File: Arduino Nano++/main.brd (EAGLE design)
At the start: 83.2 x 53.3 mm, 64 parts, among them IC1 LM358N, Q1 IRF9530, Q2 IRF9530

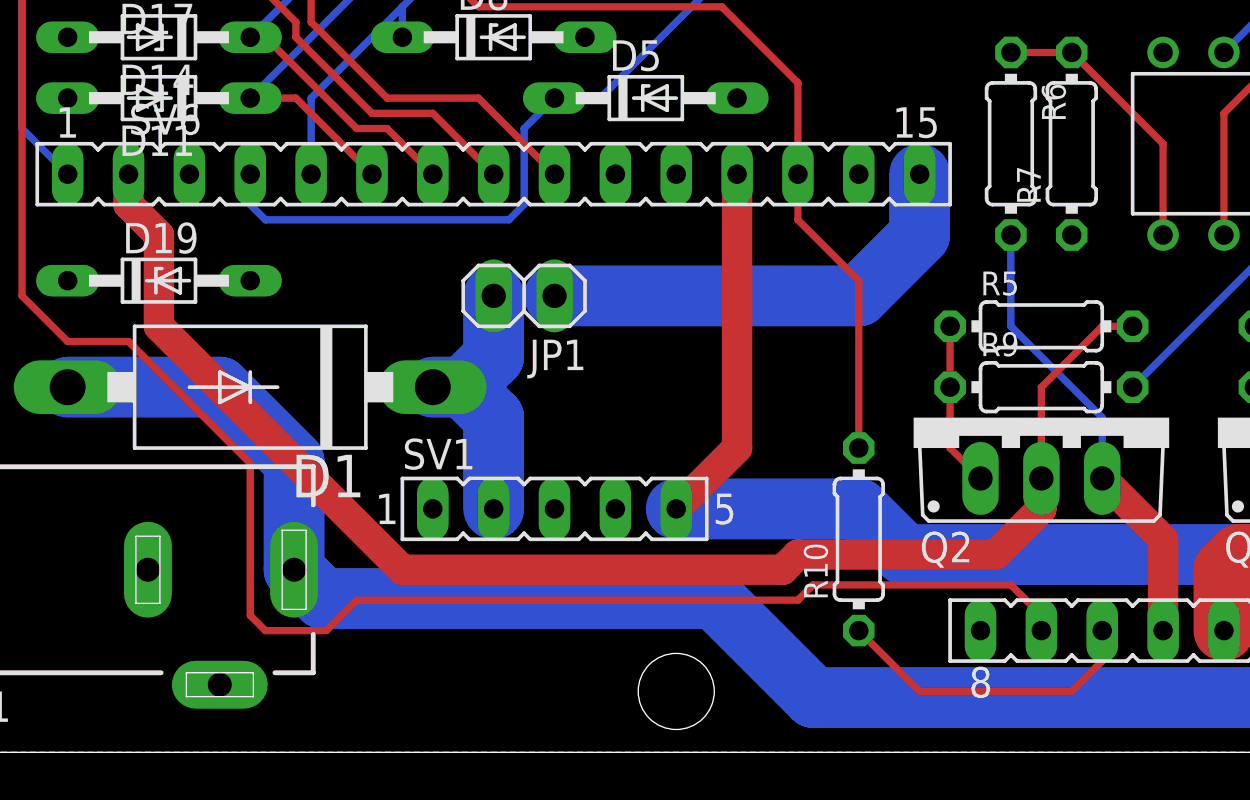
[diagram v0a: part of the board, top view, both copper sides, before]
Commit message: Increased vreg clearance
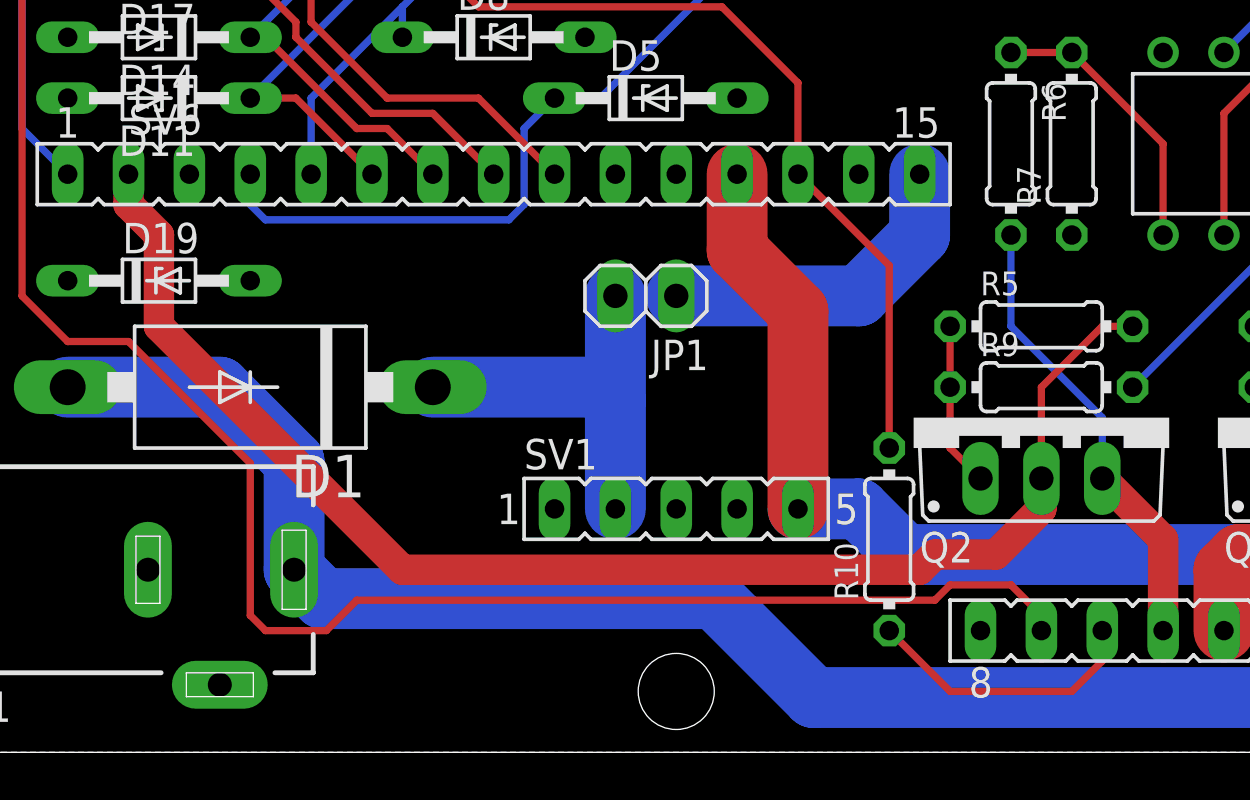
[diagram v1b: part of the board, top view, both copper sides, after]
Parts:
- moved JP1 5.08 mm to (27.9, 39.4)
- moved SV1 5.08 mm to (29.2, 30.5)
- moved R10 1.27 mm to (38.1, 29.2)
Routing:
- net N$2: track 11.2 -> 16.7 mm
- net VIN: track 18.8 -> 13.8 mm
- net 5V: track 69.8 -> 64.7 mm
- net RST': track 13.0 -> 11.7 mm
- net RST: track 46.8 -> 47.3 mm
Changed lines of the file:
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@@
 </element>
 <element name="IC1" library="linear" library_urn="urn:adsk.eagle:library:262" package="DIL08" package3d_urn="urn:adsk.eagle:package:16409/1" value="LM358N" x="53.34" y="45.72" rot="R180"/>
-<element name="JP1" library="pinhead" library_urn="urn:adsk.eagle:library:325" package="1X02" package3d_urn="urn:adsk.eagle:package:22435/2" value="" x="22.86" y="39.37" rot="R180"/>
+<element name="JP1" library="pinhead" library_urn="urn:adsk.eagle:library:325" package="1X02" package3d_urn="urn:adsk.eagle:package:22435/2" value="" x="27.94" y="39.37" rot="R180"/>
 <element name="SV6" library="con-lsta" library_urn="urn:adsk.eagle:library:161" package="FE15" package3d_urn="urn:adsk.eagle:package:8206/1" value="" x="21.59" y="44.45">
 <attribute name="MF" value="" x="21.59" y="44.45" size="1.778" layer="27" display="off"/>
@@
 <element name="R5" library="rcl" library_urn="urn:adsk.eagle:library:334" package="0204/7" package3d_urn="urn:adsk.eagle:package:23498/1" value="10k" x="44.45" y="38.1"/>
 <element name="R9" library="rcl" library_urn="urn:adsk.eagle:library:334" package="0204/7" package3d_urn="urn:adsk.eagle:package:23498/1" value="300" x="44.45" y="35.56"/>
-<element name="R10" library="rcl" library_urn="urn:adsk.eagle:library:334" package="0204/7" package3d_urn="urn:adsk.eagle:package:23498/1" value="1k" x="36.83" y="29.21" rot="R90"/>
-<element name="SV1" library="con-lsta" library_urn="urn:adsk.eagle:library:161" package="FE05-1" package3d_urn="urn:adsk.eagle:package:8190/1" value="" x="24.13" y="30.48">
-<attribute name="MF" value="" x="24.13" y="30.48" size="1.778" layer="27" display="off"/>
-<attribute name="MPN" value="" x="24.13" y="30.48" size="1.778" layer="27" display="off"/>
-<attribute name="OC_FARNELL" value="unknown" x="24.13" y="30.48" size="1.778" layer="27" display="off"/>
-<attribute name="OC_NEWARK" value="unknown" x="24.13" y="30.48" size="1.778" layer="27" display="off"/>
+<element name="R10" library="rcl" library_urn="urn:adsk.eagle:library:334" package="0204/7" package3d_urn="urn:adsk.eagle:package:23498/1" value="1k" x="38.1" y="29.21" rot="R90"/>
+<element name="SV1" library="con-lsta" library_urn="urn:adsk.eagle:library:161" package="FE05-1" package3d_urn="urn:adsk.eagle:package:8190/1" value="" x="29.21" y="30.48">
+<attribute name="MF" value="" x="29.21" y="30.48" size="1.778" layer="27" display="off"/>
+<attribute name="MPN" value="" x="29.21" y="30.48" size="1.778" layer="27" display="off"/>
+<attribute name="OC_FARNELL" value="unknown" x="29.21" y="30.48" size="1.778" layer="27" display="off"/>
+<attribute name="OC_NEWARK" value="unknown" x="29.21" y="30.48" size="1.778" layer="27" display="off"/>
 </element>
 <element name="SV3" library="con-lsta" library_urn="urn:adsk.eagle:library:161" package="FE06" package3d_urn="urn:adsk.eagle:package:8191/1" value="" x="71.12" y="25.4" rot="R180">
@@
 <wire x1="6.35" y1="43.18" x2="7.62" y2="41.91" width="1.27" layer="1"/>
 <wire x1="7.62" y1="38.1" x2="7.62" y2="41.91" width="1.27" layer="1"/>
-<wire x1="42.545" y1="28.575" x2="34.29" y2="28.575" width="1.27" layer="1"/>
 <wire x1="42.545" y1="28.575" x2="44.45" y2="30.48" width="1.27" layer="1"/>
 <wire x1="44.45" y1="31.75" x2="44.45" y2="30.48" width="1.27" layer="1"/>
-<wire x1="34.29" y1="28.575" x2="33.655" y2="27.94" width="1.27" layer="1"/>
-<wire x1="33.655" y1="27.94" x2="17.78" y2="27.94" width="1.27" layer="1"/>
-<wire x1="17.78" y1="27.94" x2="7.62" y2="38.1" width="1.27" layer="1"/>
+<wire x1="7.62" y1="38.1" x2="17.78" y2="27.94" width="1.27" layer="1"/>
 <wire x1="48.26" y1="38.1" x2="46.99" y2="38.1" width="0.3048" layer="1"/>
 <wire x1="46.99" y1="38.1" x2="44.45" y2="35.56" width="0.3048" layer="1"/>
 <wire x1="44.45" y1="35.56" x2="44.45" y2="31.75" width="0.3048" layer="1"/>
+<wire x1="39.37" y1="27.94" x2="40.005" y2="28.575" width="1.27" layer="1"/>
+<wire x1="40.005" y1="28.575" x2="42.545" y2="28.575" width="1.27" layer="1"/>
+<wire x1="17.78" y1="27.94" x2="39.37" y2="27.94" width="1.27" layer="1"/>
 </signal>
 <signal name="5V">
@@
 <contactref element="SV1" pad="5"/>
 <contactref element="IC1" pad="8"/>
-<wire x1="29.21" y1="30.48" x2="36.83" y2="30.48" width="2.54" layer="16"/>
+<wire x1="34.29" y1="30.48" x2="36.83" y2="30.48" width="2.54" layer="16"/>
 <wire x1="36.83" y1="30.48" x2="38.735" y2="28.575" width="2.54" layer="16"/>
 <wire x1="38.735" y1="28.575" x2="56.515" y2="28.575" width="2.54" layer="16"/>
 <wire x1="56.515" y1="28.575" x2="57.15" y2="29.21" width="2.54" layer="16"/>
 <wire x1="57.15" y1="29.21" x2="57.15" y2="31.75" width="2.54" layer="16"/>
-<wire x1="29.21" y1="30.48" x2="31.75" y2="33.02" width="1.27" layer="1"/>
-<wire x1="31.75" y1="33.02" x2="31.75" y2="44.45" width="1.27" layer="1"/>
 <wire x1="59.69" y1="38.1" x2="60.96" y2="38.1" width="0.3048" layer="1"/>
 <wire x1="59.69" y1="38.1" x2="57.15" y2="35.56" width="0.3048" layer="1"/>
@@
 <wire x1="60.96" y1="38.1" x2="63.5" y2="38.1" width="0.3048" layer="1"/>
 <wire x1="63.5" y1="38.1" x2="68.58" y2="43.18" width="0.3048" layer="1"/>
+<wire x1="34.29" y1="30.48" x2="34.29" y2="38.735" width="2.54" layer="1"/>
+<wire x1="34.29" y1="38.735" x2="31.75" y2="41.275" width="2.54" layer="1"/>
+<wire x1="31.75" y1="41.275" x2="31.75" y2="44.45" width="2.54" layer="1"/>
 </signal>
 <signal name="GND">
@@
 <contactref element="SV4" pad="1"/>
 <wire x1="44.45" y1="25.4" x2="44.45" y2="26.035" width="0.3048" layer="1"/>
-<wire x1="44.45" y1="26.035" x2="43.18" y2="27.305" width="0.3048" layer="1"/>
-<wire x1="43.18" y1="27.305" x2="34.925" y2="27.305" width="0.3048" layer="1"/>
-<wire x1="34.925" y1="27.305" x2="34.29" y2="26.67" width="0.3048" layer="1"/>
-<wire x1="34.29" y1="26.67" x2="15.875" y2="26.67" width="0.3048" layer="1"/>
-<wire x1="15.875" y1="26.67" x2="14.605" y2="25.4" width="0.3048" layer="1"/>
+<wire x1="43.186896875" y1="27.298103125" x2="44.45" y2="26.035" width="0.3048" layer="1"/>
+<wire x1="43.186896875" y1="27.298103125" x2="43.18" y2="27.305" width="0.3048" layer="1"/>
+<wire x1="14.605" y1="25.4" x2="15.875" y2="26.67" width="0.3048" layer="1"/>
 <wire x1="14.605" y1="25.4" x2="12.065" y2="25.4" width="0.3048" layer="1"/>
 <wire x1="12.065" y1="25.4" x2="11.43" y2="26.035" width="0.3048" layer="1"/>
@@
 <wire x1="33.655" y1="66.675" x2="38.1" y2="71.12" width="0.3048" layer="1"/>
 <wire x1="1.905" y1="39.37" x2="1.905" y2="64.77" width="0.3048" layer="1"/>
+<wire x1="40.005" y1="26.67" x2="40.64" y2="27.305" width="0.3048" layer="1"/>
+<wire x1="40.64" y1="27.305" x2="43.18" y2="27.305" width="0.3048" layer="1"/>
+<wire x1="43.18" y1="27.305" x2="43.186896875" y2="27.298103125" width="0.3048" layer="1"/>
+<wire x1="15.875" y1="26.67" x2="40.005" y2="26.67" width="0.3048" layer="1"/>
 </signal>
 <signal name="RST'">
@@
 <contactref element="R10" pad="1"/>
 <wire x1="46.99" y1="25.4" x2="46.99" y2="24.13" width="0.3048" layer="1"/>
-<wire x1="46.99" y1="24.13" x2="45.72" y2="22.86" width="0.3048" layer="1"/>
-<wire x1="45.72" y1="22.86" x2="39.37" y2="22.86" width="0.3048" layer="1"/>
-<wire x1="39.37" y1="22.86" x2="36.83" y2="25.4" width="0.3048" layer="1"/>
+<wire x1="45.72" y1="22.86" x2="46.99" y2="24.13" width="0.3048" layer="1"/>
+<wire x1="38.1" y1="25.4" x2="40.64" y2="22.86" width="0.3048" layer="1"/>
+<wire x1="40.64" y1="22.86" x2="45.72" y2="22.86" width="0.3048" layer="1"/>
 </signal>
 <signal name="RST">
@@
 <wire x1="31.115" y1="51.435" x2="34.29" y2="48.26" width="0.3048" layer="1"/>
 <wire x1="34.29" y1="44.45" x2="34.29" y2="48.26" width="0.3048" layer="1"/>
-<wire x1="36.83" y1="33.02" x2="36.83" y2="40.005" width="0.3048" layer="1"/>
-<wire x1="36.83" y1="40.005" x2="34.29" y2="42.545" width="0.3048" layer="1"/>
-<wire x1="34.29" y1="42.545" x2="34.29" y2="44.45" width="0.3048" layer="1"/>
+<wire x1="38.1" y1="33.02" x2="38.1" y2="40.64" width="0.3048" layer="1"/>
+<wire x1="38.1" y1="40.64" x2="34.29" y2="44.45" width="0.3048" layer="1"/>
 </signal>
 <signal name="VREF2.4">
@@
 <contactref element="JP1" pad="2"/>
 <contactref element="SV1" pad="2"/>
-<wire x1="20.32" y1="35.56" x2="19.05" y2="35.56" width="2.54" layer="16"/>
-<wire x1="20.32" y1="35.56" x2="21.59" y2="34.29" width="2.54" layer="16"/>
-<wire x1="21.59" y1="34.29" x2="21.59" y2="30.48" width="2.54" layer="16"/>
-<wire x1="21.59" y1="39.37" x2="21.59" y2="36.83" width="2.54" layer="16"/>
-<wire x1="21.59" y1="36.83" x2="20.32" y2="35.56" width="2.54" layer="16"/>
+<wire x1="26.67" y1="35.010121875" x2="26.67" y2="39.37" width="2.54" layer="16"/>
+<wire x1="26.67" y1="35.010121875" x2="26.67" y2="30.48" width="2.54" layer="16"/>
+<wire x1="19.05" y1="35.56" x2="26.120121875" y2="35.56" width="2.54" layer="16"/>
+<wire x1="26.120121875" y1="35.56" x2="26.67" y2="35.010121875" width="2.54" layer="16"/>
 </signal>
 <signal name="VIN">
 <contactref element="JP1" pad="1"/>
 <contactref element="SV6" pad="15"/>
-<wire x1="24.13" y1="39.37" x2="36.83" y2="39.37" width="2.54" layer="16"/>
+<wire x1="29.21" y1="39.37" x2="36.83" y2="39.37" width="2.54" layer="16"/>
 <wire x1="36.83" y1="39.37" x2="39.37" y2="41.91" width="2.54" layer="16"/>
 <wire x1="39.37" y1="41.91" x2="39.37" y2="44.45" width="2.54" layer="16"/>

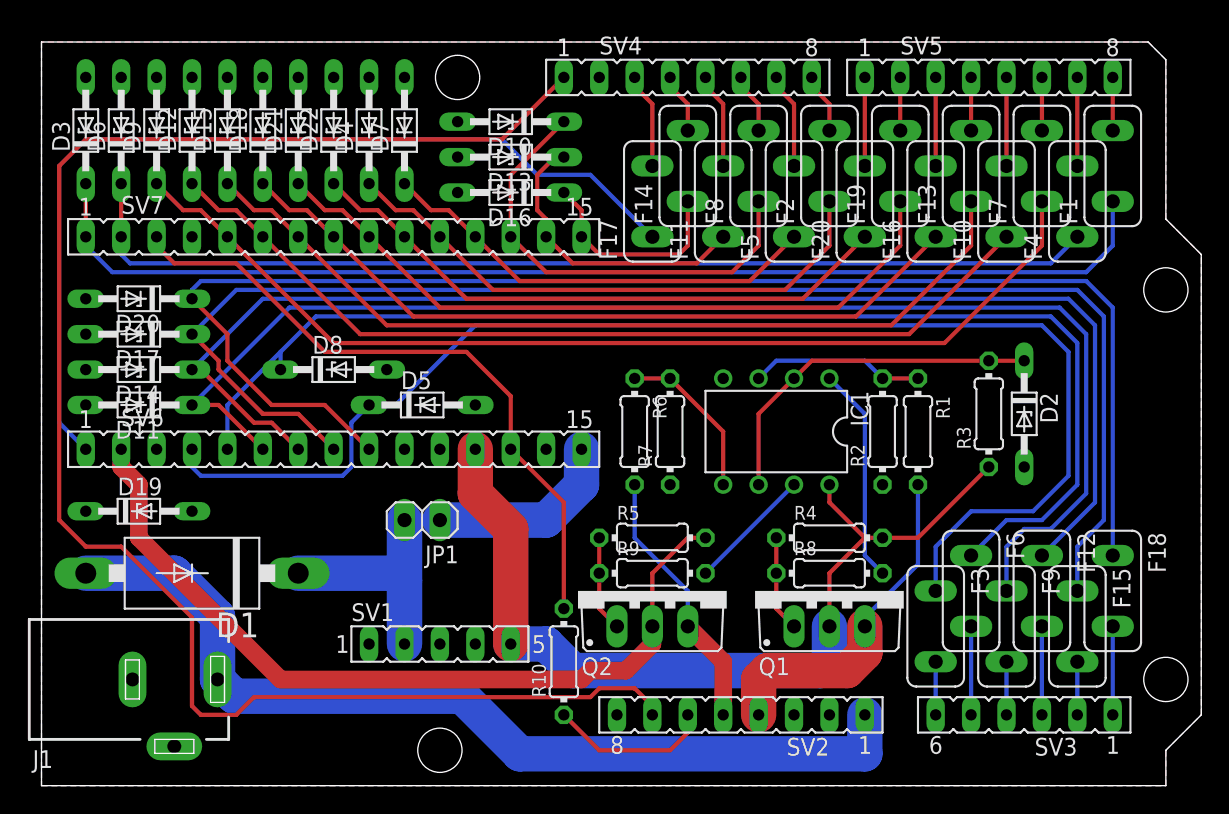
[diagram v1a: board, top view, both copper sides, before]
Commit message: Removed vreg slot
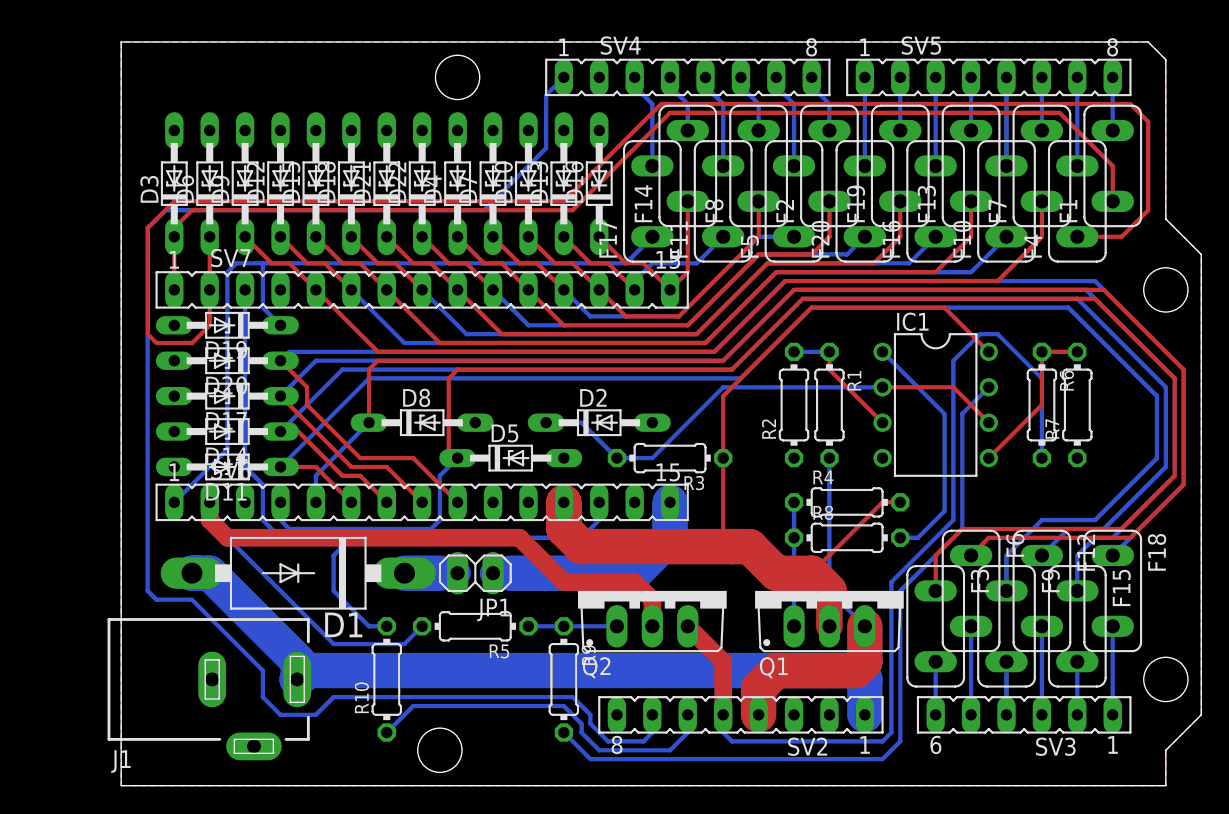
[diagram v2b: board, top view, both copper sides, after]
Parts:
- removed SV1: (no value), con-lsta:FE05-1
- moved D2 30.5 mm to (40.6, 46.4), turned to 0 degrees
- moved R7 29.3 mm to (74.9, 47.6)
- moved R6 29.3 mm to (72.4, 47.6)
- moved R3 23.1 mm to (45.7, 43.8), turned to 180 degrees
- moved D19 14.8 mm to (14.0, 53.3), turned to 180 degrees
- moved R5 14.2 mm to (31.8, 31.8), turned to 180 degrees
- moved R10 12.8 mm to (25.4, 27.9)
- moved IC1 11.6 mm to (64.8, 47.6), turned to 270 degrees
- moved R9 9.92 mm to (38.1, 27.9), turned to 270 degrees
- moved D11 7.75 mm to (14.0, 43.2)
- moved D14 7.75 mm to (14.0, 45.7)
- moved D17 7.75 mm to (14.0, 48.3)
- moved D20 7.75 mm to (14.0, 50.8)
- moved D1 7.62 mm to (19.1, 35.6)
- moved D12 7.41 mm to (17.8, 63.5)
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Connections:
- net 5V: no longer SV1.5
- net GND: no longer SV1.3, SV1.4
- net N$2: no longer SV1.2
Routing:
- net 3V3': track 19.1 -> 63.9 mm
- net 3V3EN: track 8.98 -> 53.5 mm
- net D1: track 74.7 -> 107.4 mm
- net A0: track 95.2 -> 110.0 mm
- net RST': track 11.7 -> 25.9 mm
- net N$2: track 16.7 -> 3.81 mm
- net D13: track 67.3 -> 54.6 mm
- net A1: track 88.7 -> 99.9 mm
- net AREF': track 118.2 -> 107.3 mm
- net VIN': track 66.7 -> 55.9 mm
- net VREF2.4: track 25.7 -> 36.0 mm
- net D10: track 32.6 -> 23.8 mm
- net D2: track 74.3 -> 66.5 mm
- net D3: track 65.8 -> 58.4 mm
- net D4: track 63.1 -> 55.8 mm
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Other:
- board size 83.2 x 53.3 mm -> 77.5 x 53.3 mm
